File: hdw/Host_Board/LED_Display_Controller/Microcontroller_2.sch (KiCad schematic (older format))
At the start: 1 part

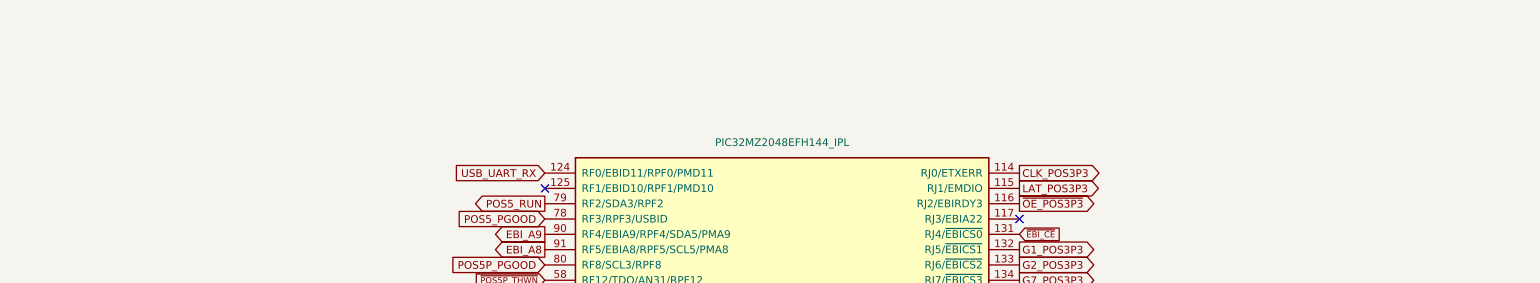
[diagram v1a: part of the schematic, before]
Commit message: Added titles and MU logo to each sheet
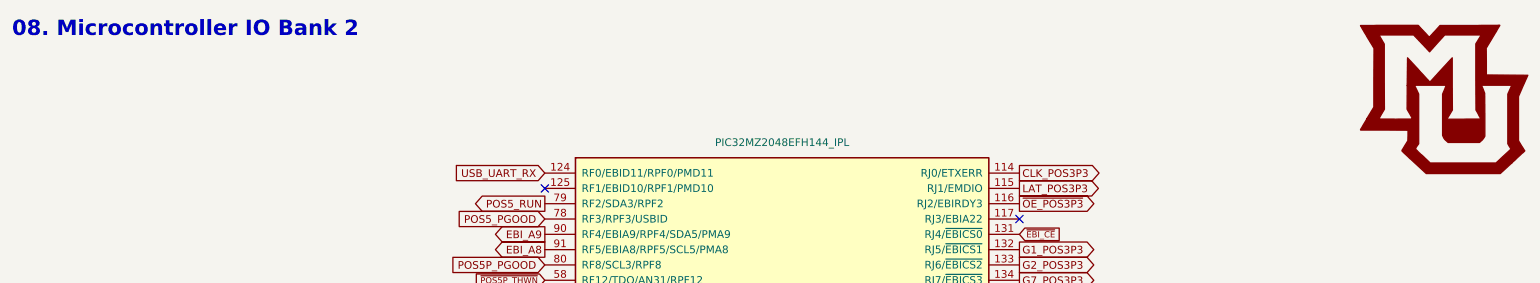
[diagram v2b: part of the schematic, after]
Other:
- note added: "08. Microcontroller IO Bank 2"
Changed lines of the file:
@@
 NoConn ~ 4030 4180
 NoConn ~ 7130 1880
+Text Notes 550  700  0    100  ~ 20
+08. Microcontroller IO Bank 2
+$Comp
+L LED_Display_Local_Library:MU_Logo #G?
+U 1 1 5BFF2FC2
+P 9900 1100
+F 0 "#G?" H 9900 614 60  0001 C CNN
+F 1 "MU_Logo" H 9900 1586 60  0001 C CNN
+F 2 "" H 9900 1100 50  0001 C CNN
+F 3 "" H 9900 1100 50  0001 C CNN
+	1    9900 1100
+	1    0    0    -1
+$EndComp
 $EndSCHEMATC
